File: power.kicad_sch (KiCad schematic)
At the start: 0 parts

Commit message: Created 1v5 to 3v3 boost schematic for MCU
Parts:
- added 3V3: TestPoint, TestPoint:TestPoint_Pad_2.0x2.0mm, symbol Connector:TestPoint
- added BT1: 1.5V, Battery:BatteryHolder_Keystone_2460_1xAA, symbol Device:Battery_Cell
- added C1: 22uF, Capacitor_SMD:C_0805_2012Metric_Pad1.18x1.45mm_HandSolder, symbol Device:C
- added C2: 10uF, Capacitor_SMD:C_0805_2012Metric_Pad1.18x1.45mm_HandSolder, symbol Device:C
- added L1: 470nH, Inductor_SMD:L_Coilcraft_XxL4020, symbol Device:L
- added R1: 100K, Resistor_SMD:R_0805_2012Metric_Pad1.20x1.40mm_HandSolder, symbol Device:R_US
- added R2: 511K, Resistor_SMD:R_0805_2012Metric_Pad1.20x1.40mm_HandSolder, symbol Device:R_US
- added R3: 91K, Resistor_SMD:R_0805_2012Metric_Pad1.20x1.40mm_HandSolder, symbol Device:R_US
- added U1: TPS63802DLAR, TPS63802DLAR:DLA0010A, symbol TPS63802DLAR:TPS63802DLAR
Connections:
- new net: R2.1, R3.2, U1.4 (FB)
- new net: L1.1, U1.9 (L1)
- new net: L1.2, U1.7 (L2)
- new net: R1.1, U1.5 (PG)
- new net: BT1.1 (+), C2.1, U1.1 (EN), U1.10 (VIN)
- new net 3V3: 3V3.1, C1.1, R1.2, R2.2, U1.6 (VOUT)
- new net GND: BT1.2 (-), C1.2, C2.2, R3.1, U1.2 (MODE), U1.3 (AGND), U1.8 (GND)

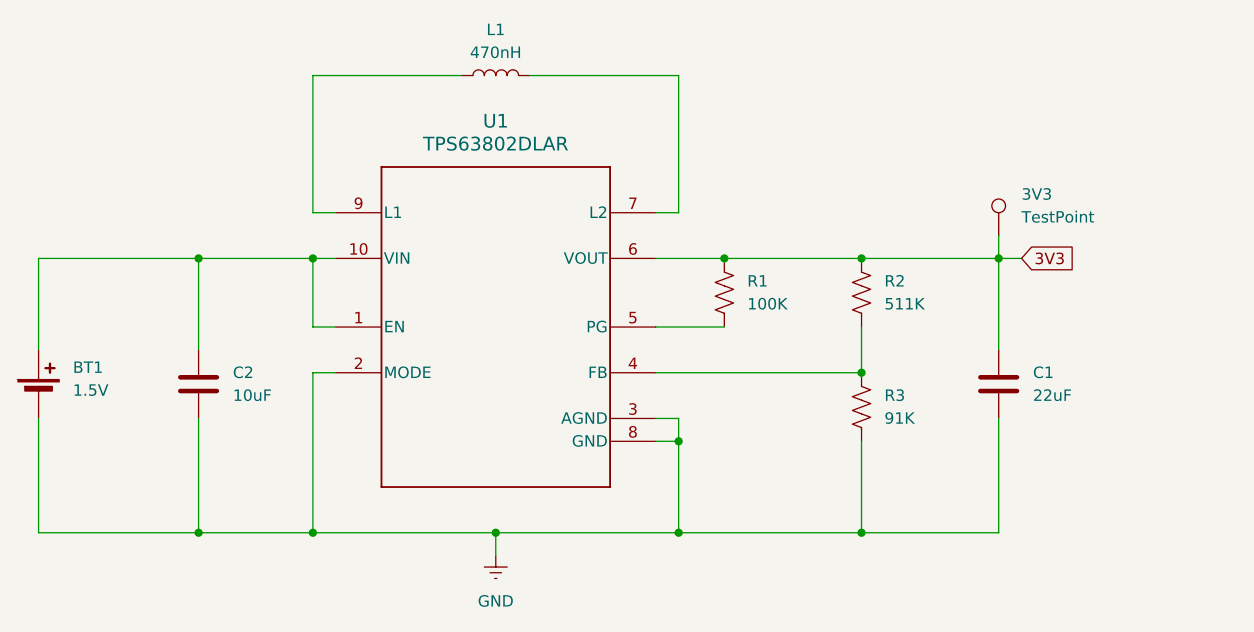
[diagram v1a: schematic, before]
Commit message: Updated boost converter to output 5v instead of 3v3 for ESP32 dev board
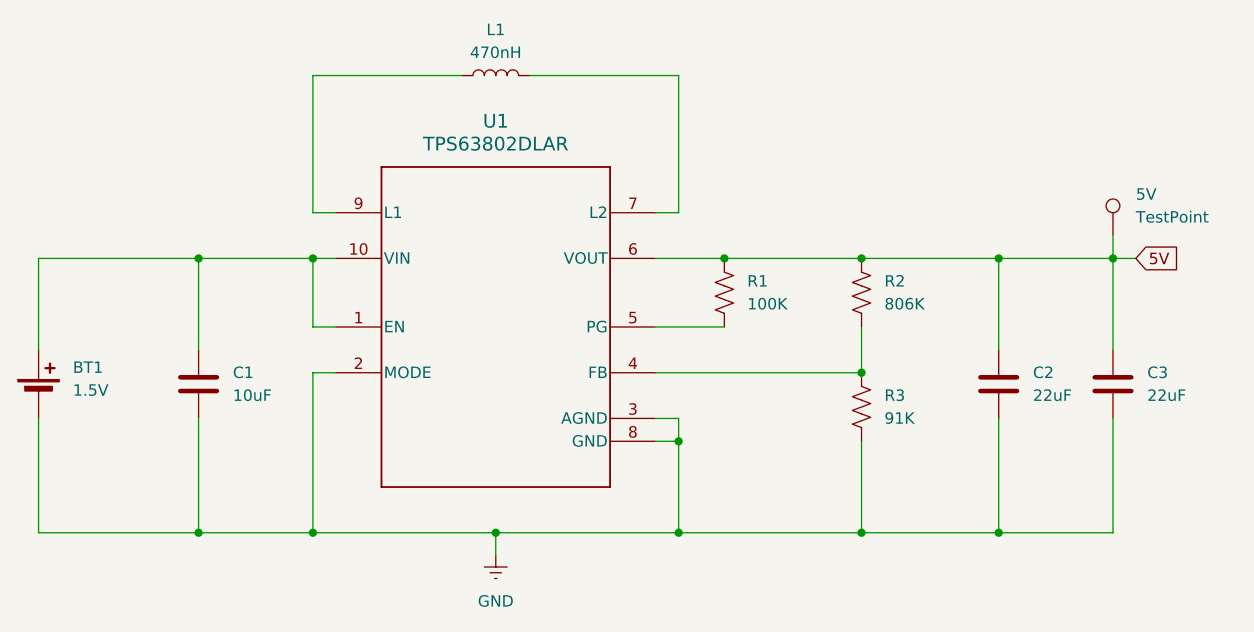
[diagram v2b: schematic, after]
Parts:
- added C3: 22uF, Capacitor_SMD:C_0805_2012Metric_Pad1.18x1.45mm_HandSolder, symbol Device:C
- R2: value 511K -> 806K
- renumbered 3V3 to 5V, C2 to C1, C1 to C2
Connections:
- net GND: now also C3.2
- net 3V3 renamed 5V
- net 5V: now also C3.1
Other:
- moved on the sheet: 5V
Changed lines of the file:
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@@
 	(paper "A4")
 	(junction
+		(at 111.76 59.69)
+		(diameter 0)
+		(color 0 0 0 0)
+	)
+	(junction
+		(at 127 90.17)
+		(diameter 0)
+		(color 0 0 0 0)
+	)
+	(junction
+		(at 66.04 90.17)
+		(diameter 0)
+		(color 0 0 0 0)
+	)
+	(junction
+		(at 106.68 80.01)
+		(diameter 0)
+		(color 0 0 0 0)
+	)
+	(junction
+		(at 53.34 59.69)
+		(diameter 0)
+		(color 0 0 0 0)
+	)
+	(junction
+		(at 86.36 90.17)
+		(diameter 0)
+		(color 0 0 0 0)
+	)
+	(junction
+		(at 106.68 90.17)
+		(diameter 0)
+		(color 0 0 0 0)
+	)
+	(junction
+		(at 53.34 90.17)
+		(diameter 0)
+		(color 0 0 0 0)
+	)
+	(junction
+		(at 127 72.39)
+		(diameter 0)
+		(color 0 0 0 0)
+	)
+	(junction
+		(at 142.24 90.17)
+		(diameter 0)
+		(color 0 0 0 0)
+	)
+	(junction
 		(at 142.24 59.69)
 		(diameter 0)
@@
 	)
 	(junction
-		(at 111.76 59.69)
-		(diameter 0)
-		(color 0 0 0 0)
-	)
-	(junction
-		(at 127 90.17)
-		(diameter 0)
-		(color 0 0 0 0)
-	)
-	(junction
-		(at 66.04 90.17)
-		(diameter 0)
-		(color 0 0 0 0)
-	)
-	(junction
 		(at 127 59.69)
 		(diameter 0)
@@
 	)
 	(junction
-		(at 106.68 80.01)
-		(diameter 0)
-		(color 0 0 0 0)
-	)
-	(junction
-		(at 53.34 59.69)
-		(diameter 0)
-		(color 0 0 0 0)
-	)
-	(junction
-		(at 86.36 90.17)
-		(diameter 0)
-		(color 0 0 0 0)
-	)
-	(junction
-		(at 106.68 90.17)
-		(diameter 0)
-		(color 0 0 0 0)
-	)
-	(junction
-		(at 53.34 90.17)
-		(diameter 0)
-		(color 0 0 0 0)
-	)
-	(junction
-		(at 127 72.39)
+		(at 154.94 59.69)
 		(diameter 0)
 		(color 0 0 0 0)
@@
 	(wire
 		(pts
+			(xy 154.94 59.69) (xy 154.94 69.85)
+		)
+		(stroke
+			(width 0)
+			(type default)
+		)
+	)
+	(wire
+		(pts
 			(xy 106.68 90.17) (xy 86.36 90.17)
 		)
@@
 	(wire
 		(pts
-			(xy 142.24 59.69) (xy 144.78 59.69)
+			(xy 154.94 59.69) (xy 157.48 59.69)
 		)
 		(stroke
@@
 	(wire
 		(pts
-			(xy 142.24 57.15) (xy 142.24 59.69)
+			(xy 154.94 57.15) (xy 154.94 59.69)
 		)
 		(stroke
@@
 	(wire
 		(pts
+			(xy 127 59.69) (xy 142.24 59.69)
+		)
+		(stroke
+			(width 0)
+			(type default)
+		)
+	)
+	(wire
+		(pts
+			(xy 142.24 59.69) (xy 154.94 59.69)
+		)
+		(stroke
+			(width 0)
+			(type default)
+		)
+	)
+	(wire
+		(pts
 			(xy 35.56 69.85) (xy 35.56 59.69)
 		)
@@
 	(wire
 		(pts
-			(xy 127 59.69) (xy 142.24 59.69)
-		)
-		(stroke
-			(width 0)
-			(type default)
-		)
-	)
-	(wire
-		(pts
 			(xy 86.36 90.17) (xy 86.36 92.71)
 		)
@@
 	(wire
 		(pts
+			(xy 154.94 90.17) (xy 154.94 77.47)
+		)
+		(stroke
+			(width 0)
+			(type default)
+		)
+	)
+	(wire
+		(pts
 			(xy 53.34 59.69) (xy 53.34 69.85)
 		)
@@
 	(wire
 		(pts
+			(xy 142.24 90.17) (xy 154.94 90.17)
+		)
+		(stroke
+			(width 0)
+			(type default)
+		)
+	)
+	(wire
+		(pts
 			(xy 104.14 72.39) (xy 127 72.39)
 		)
@@
 		)
 	)
-	(global_label "3V3"
+	(global_label "5V"
 		(shape input)
-		(at 144.78 59.69 0)
+		(at 157.48 59.69 0)
 		(fields_autoplaced yes)
 		(effects
@@
 		)
 		(property "Intersheetrefs" "${INTERSHEET_REFS}"
-			(at 151.2728 59.69 0)
+			(at 162.7633 59.69 0)
 			(effects
 				(font
@@
 		(dnp no)
 		(fields_autoplaced yes)
-		(property "Reference" "C1"
+		(property "Reference" "C2"
 			(at 146.05 72.3899 0)
 			(effects
@@
 			(project ""
 				(path "/225cfa82-97e7-4320-90e1-4d94ef39f9f2/9d03af3c-7e27-487a-be84-d59389aa1574"
-					(reference "C1")
+					(reference "C2")
 					(unit 1)
 				)
@@
 			)
 		)
-		(property "Value" "511K"
+		(property "Value" "806K"
 			(at 129.54 64.7699 0)
 			(effects
@@
 	(symbol
 		(lib_id "Connector:TestPoint")
-		(at 142.24 57.15 0)
+		(at 154.94 57.15 0)
 		(unit 1)
 		(exclude_from_sim no)
@@
 		(dnp no)
 		(fields_autoplaced yes)
-		(property "Reference" "3V3"
-			(at 144.78 52.5779 0)
+		(property "Reference" "5V"
+			(at 157.48 52.5779 0)
 			(effects
 				(font
@@
 		)
 		(property "Value" "TestPoint"
-			(at 144.78 55.1179 0)
+			(at 157.48 55.1179 0)
 			(effects
 				(font
@@
 		)
 		(property "Footprint" "TestPoint:TestPoint_Pad_2.0x2.0mm"
-			(at 147.32 57.15 0)
+			(at 160.02 57.15 0)
 			(effects
 				(font
@@
 		)
 		(property "Datasheet" "~"
-			(at 147.32 57.15 0)
+			(at 160.02 57.15 0)
 			(effects
 				(font
@@
 		)
 		(property "Description" "test point"
-			(at 142.24 57.15 0)
+			(at 154.94 57.15 0)
 			(effects
 				(font
@@
 			(project ""
 				(path "/225cfa82-97e7-4320-90e1-4d94ef39f9f2/9d03af3c-7e27-487a-be84-d59389aa1574"
-					(reference "3V3")
+					(reference "5V")
 					(unit 1)
 				)
@@
 	(symbol
 		(lib_id "Device:C")
+		(at 154.94 73.66 0)
+		(unit 1)
+		(exclude_from_sim no)
+		(in_bom yes)
+		(on_board yes)
+		(dnp no)
+		(fields_autoplaced yes)
+		(property "Reference" "C3"
+			(at 158.75 72.3899 0)
+			(effects
+				(font
+					(size 1.27 1.27)
+				)
+				(justify left)
+			)
+		)
+		(property "Value" "22uF"
+			(at 158.75 74.9299 0)
+			(effects
+				(font
+					(size 1.27 1.27)
+				)
+				(justify left)
+			)
+		)
+		(property "Footprint" "Capacitor_SMD:C_0805_2012Metric_Pad1.18x1.45mm_HandSolder"
+			(at 155.9052 77.47 0)
+			(effects
+				(font
+					(size 1.27 1.27)
+				)
+				(hide yes)
+			)
+		)
+		(property "Datasheet" "~"
+			(at 154.94 73.66 0)
+			(effects
+				(font
+					(size 1.27 1.27)
+				)
+				(hide yes)
+			)
+		)
+		(property "Description" "Unpolarized capacitor"
+			(at 154.94 73.66 0)
+			(effects
+				(font
+					(size 1.27 1.27)
+				)
+				(hide yes)
+			)
+		)
+		(pin "2"
+		)
+		(pin "1"
+		)
+		(instances
+			(project "FES_Hardware"
+				(path "/225cfa82-97e7-4320-90e1-4d94ef39f9f2/9d03af3c-7e27-487a-be84-d59389aa1574"
+					(reference "C3")
+					(unit 1)
+				)
+			)
+		)
+	)
+	(symbol
+		(lib_id "Device:C")
 		(at 53.34 73.66 0)
 		(unit 1)
@@
 		(dnp no)
 		(fields_autoplaced yes)
-		(property "Reference" "C2"
+		(property "Reference" "C1"
 			(at 57.15 72.3899 0)
 			(effects
@@
 			(project "FES_Hardware"
 				(path "/225cfa82-97e7-4320-90e1-4d94ef39f9f2/9d03af3c-7e27-487a-be84-d59389aa1574"
-					(reference "C2")
+					(reference "C1")
 					(unit 1)
 				)
